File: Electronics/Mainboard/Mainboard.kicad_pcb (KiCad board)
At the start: 2 copper layers, 160 x 120 mm, 191 parts, among them J1 609-5192-ND, J2 DB25_Male_MountingHoles, J3 609-5192-ND, J4 609-5192-ND, U1 AD8676, U10 AD8675, U11 AD5781, U12 AD8676xR, U13 AD8675, U14 LM75C, U15 Beaglebone_Black, U16 AD5781, U17 AD8676xR, U18 AD8675, U19 ADP7142AUJZ-5.0, U2 AD8676, U20 ADR4550, U21 AD8676, U22 AD8675, U3 LT1469, U4 LTC2338-18, U5 AD5781, U6 AD8676xR, U7 AD8675, U8 AD5781, U9 AD8676xR

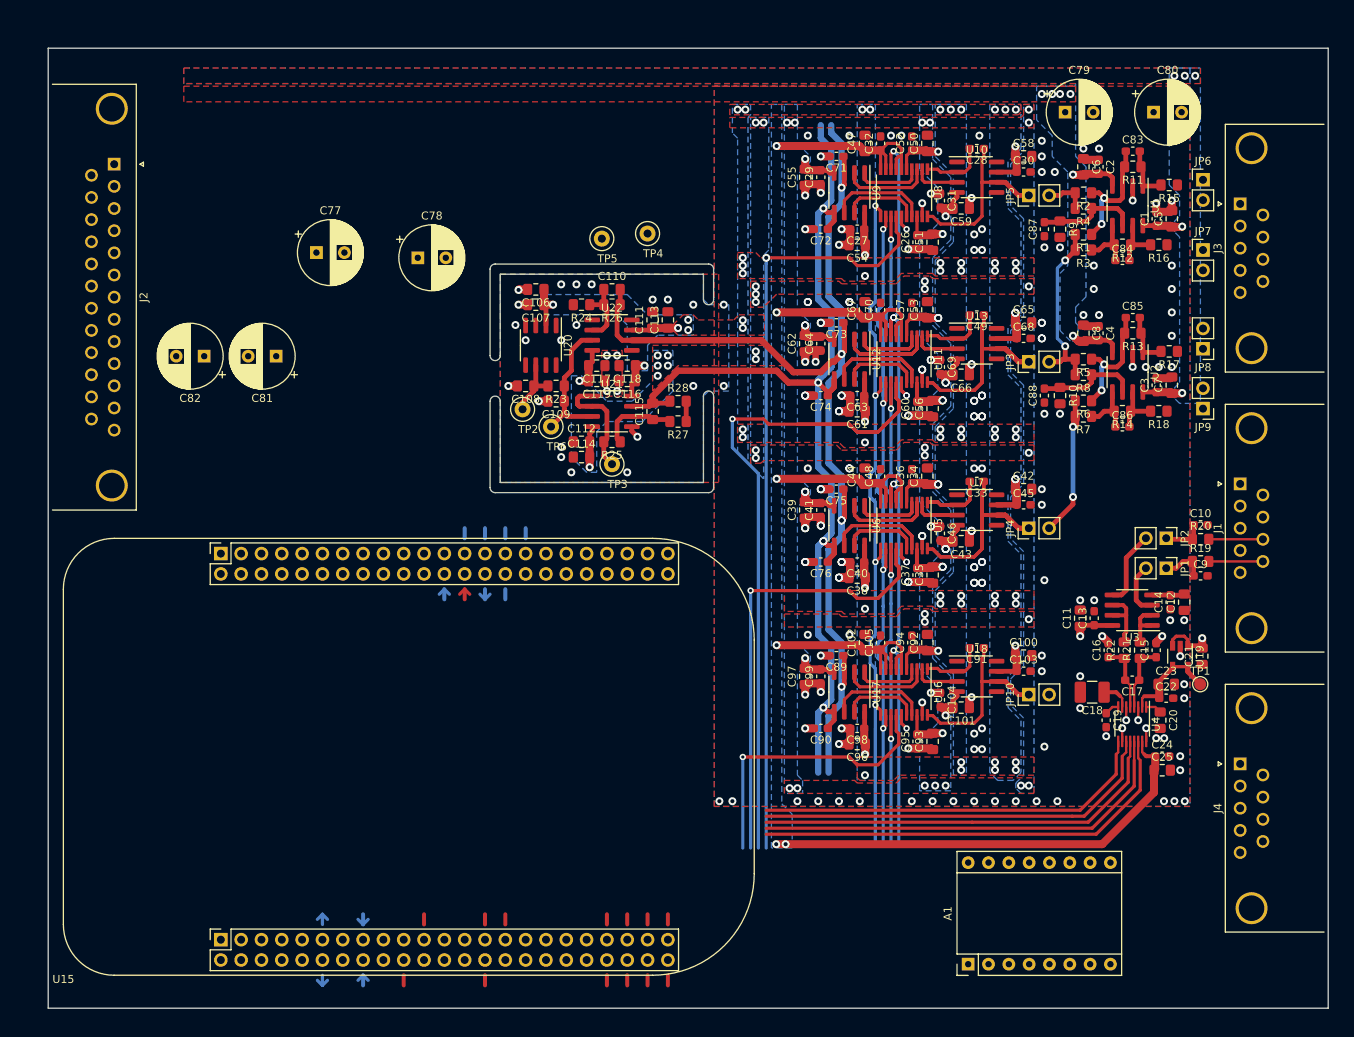
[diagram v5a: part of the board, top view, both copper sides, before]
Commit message: SPI Connections finished
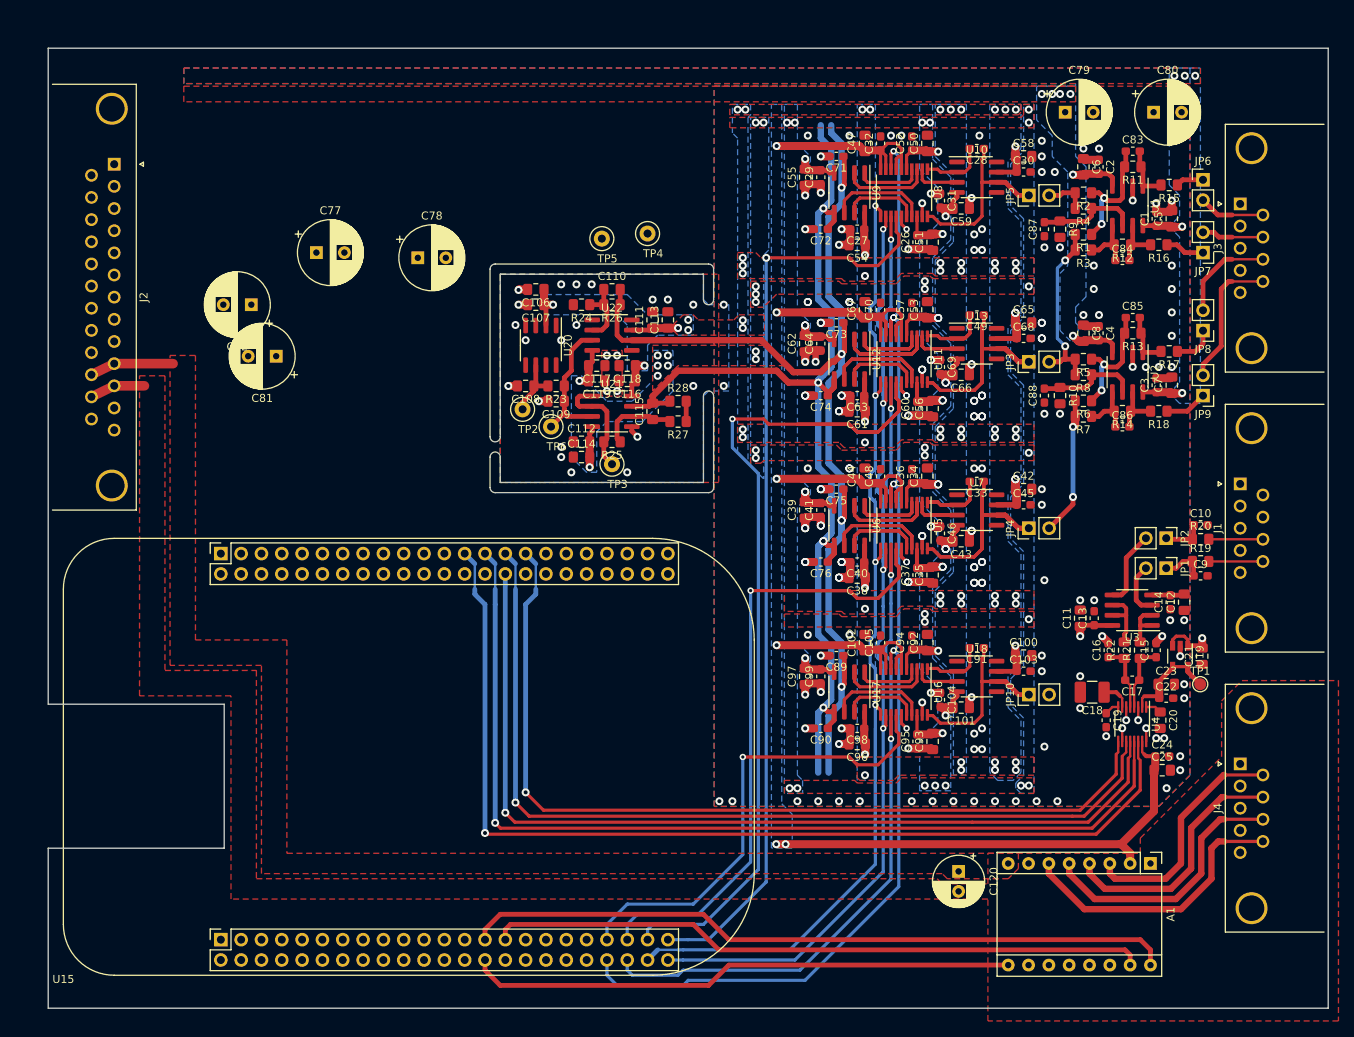
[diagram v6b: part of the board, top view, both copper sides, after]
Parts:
- added C120: 100u 35V, Capacitor_THT:CP_Radial_D6.3mm_P2.50mm, F.Cu at (183.8, 142.9)
- moved A1 26.0 mm to (207.8, 141.9), turned to 270 degrees
- moved C82 8.73 mm to (95.4, 72.1)
- moved JP8 2.28 mm to (214.3, 75.3)
- moved JP9 1.62 mm to (214.3, 83.4)
- moved JP7 0.33 mm to (214.3, 65.5), turned to 180 degrees
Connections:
- A1 pad 15: /Stepper-Driver/STEP -> /Beaglebone/Motor-Step
- J4 pad 6: /Stepper-Driver/B- -> /Stepper-Driver/A+
- J4 pad 7: /Stepper-Driver/B+ -> /Stepper-Driver/A-
- J4 pad 8: /Stepper-Driver/A- -> /Stepper-Driver/B+
- J4 pad 9: /Stepper-Driver/A+ -> /Stepper-Driver/B-
- U15 pad P8_27: Net-(U15-PadP8_27) -> /Stepper-Driver/DIR
- U15 pad P8_28: Net-(U15-PadP8_28) -> /Stepper-Driver/~ENABLE
- U15 pad P8_29: Net-(U15-PadP8_29) -> /Beaglebone/Motor-Step
- U15 pad P8_39: Net-(U15-PadP8_39) -> /~DAC_CS-Bias
- U15 pad P8_40: Net-(U15-PadP8_40) -> /~DAC_LDAC
- U15 pad P8_41: Net-(U15-PadP8_41) -> /~DAC_CS-Y
- U15 pad P8_42: Net-(U15-PadP8_42) -> /DAC_CLK
- U15 pad P8_43: Net-(U15-PadP8_43) -> /~DAC_CS-Z
- U15 pad P8_44: Net-(U15-PadP8_44) -> /DAC_MISO
- U15 pad P8_45: Net-(U15-PadP8_45) -> /~DAC_CS-X
- U15 pad P8_46: Net-(U15-PadP8_46) -> /DAC_MOSI
- U15 pad P9_25: Net-(U15-PadP9_25) -> /ADC_MISO
- U15 pad P9_27: Net-(U15-PadP9_27) -> /ADC_CLK
- U15 pad P9_29: Net-(U15-PadP9_29) -> /ADC_BUSY
- U15 pad P9_30: Net-(U15-PadP9_30) -> /ADC_MOSI
- U15 pad P9_31: Net-(U15-PadP9_31) -> /ADC_CONV
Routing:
- net /Stepper-Driver/DIR: track 0.00 -> 89.0 mm
- net /Beaglebone/Motor-Step: track 0.00 -> 82.5 mm
- net /ADC_MISO: track 55.2 -> 126.4 mm, vias 0 -> 1
- net /Stepper-Driver/~ENABLE: track 0.00 -> 68.5 mm
- net /ADC_CLK: track 53.8 -> 122.1 mm, vias 0 -> 1
- net /ADC_BUSY: track 51.3 -> 115.0 mm, vias 0 -> 1
- net /ADC_MOSI: track 52.5 -> 115.5 mm, vias 0 -> 1
- net /ADC_CONV: track 49.8 -> 111.7 mm, vias 0 -> 1
- net /~DAC_LDAC: track 106.3 -> 155.8 mm
- net (no net): track 44.3 -> 0.00 mm
- net /DAC_CLK: track 115.0 -> 159.1 mm
- net /DAC_MISO: track 132.8 -> 168.9 mm
- net /Stepper-Driver/B-: track 0.00 -> 35.6 mm
- net /DAC_MOSI: track 111.0 -> 146.1 mm
- net /Stepper-Driver/B+: track 0.00 -> 33.5 mm
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- added copper zone on F.Cu, net /9V
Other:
- outline, holes or cut-outs redrawn

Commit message: Further layout stuff
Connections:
- J1 pad 1: /+15V -> /-15V
- J1 pad 6: /-15V -> /+15V
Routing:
- net /Bias: track 0.00 -> 43.1 mm
- net /GND: track 156.9 -> 161.0 mm, vias 199 -> 205
- net /-15V: track 107.3 -> 109.5 mm, vias 56 -> 59
- net /+15V: vias 74 -> 80

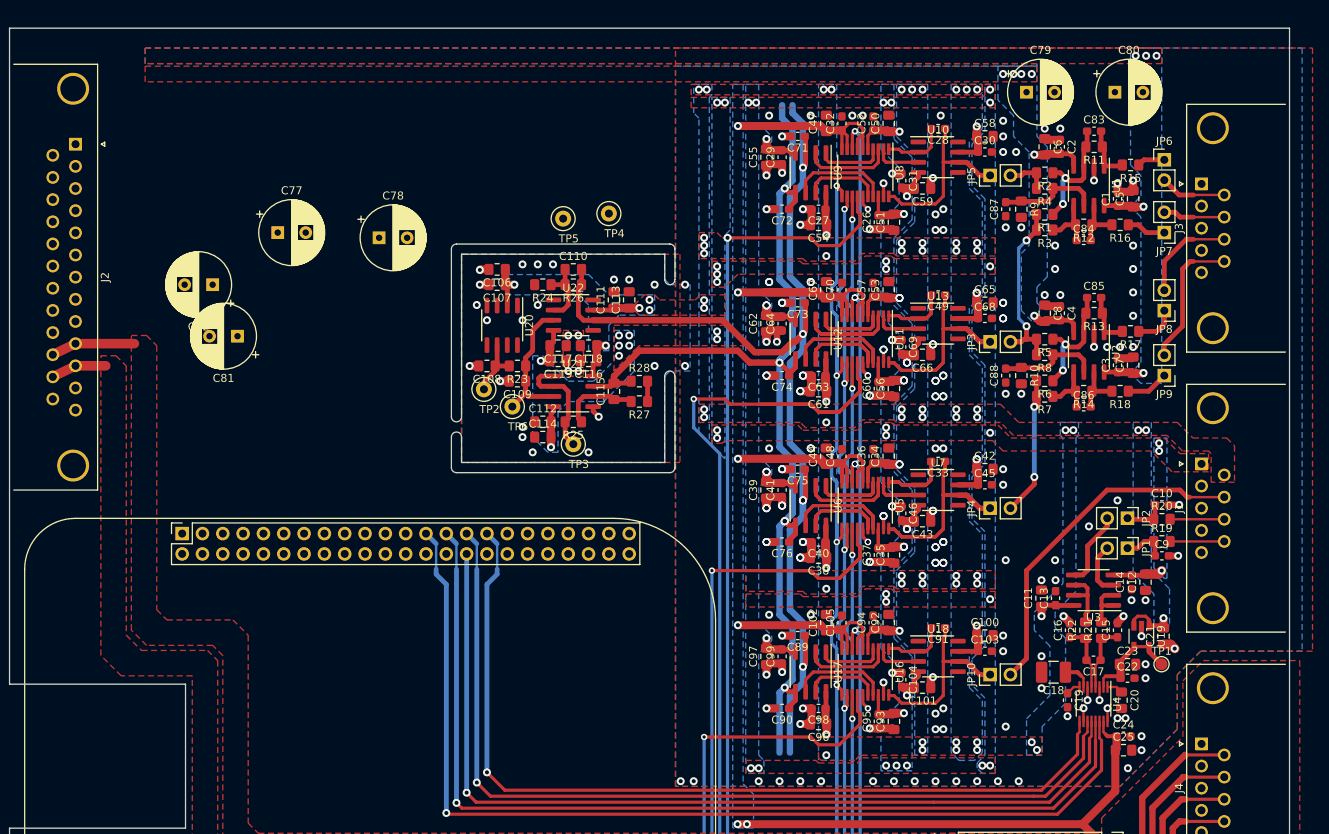
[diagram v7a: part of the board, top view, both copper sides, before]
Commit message: Power supply routing progress
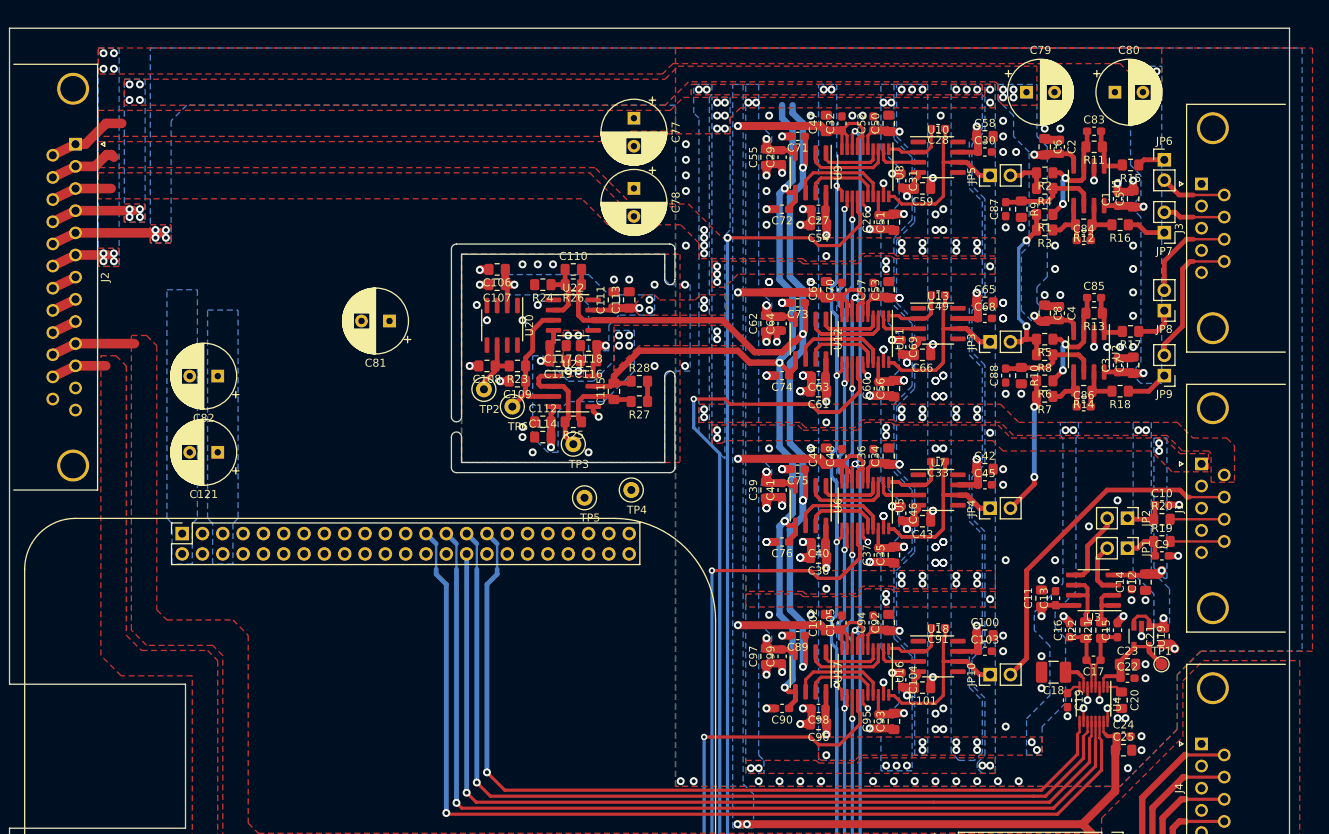
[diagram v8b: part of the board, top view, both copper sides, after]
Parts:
- added C121: 330u 16V, Capacitor_THT:CP_Radial_D8.0mm_P3.50mm, F.Cu at (96.0, 93.0)
- moved C77 46.8 mm to (148.1, 51.2), turned to 270 degrees
- moved TP5 35.0 mm to (141.9, 98.7)
- moved TP4 34.7 mm to (147.7, 97.7)
- moved C78 32.4 mm to (148.1, 60.0), turned to 270 degrees
- moved C81 19.1 mm to (117.5, 76.6)
- moved C82 11.4 mm to (96.0, 83.5)
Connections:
- C82 pad 1: /GND -> /5V
- C82 pad 2: /Beaglebone/5V -> /GND
- J2 pad 22: /Beaglebone/5V -> /5V
- J2 pad 9: /Beaglebone/5V -> /5V
- U15 pad P9_5: /Beaglebone/5V -> /5V
- U15 pad P9_6: /Beaglebone/5V -> /5V
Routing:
- net /GND: track 161.0 -> 186.6 mm, vias 205 -> 216
- net /REF_P: track 166.7 -> 155.3 mm
- net /-20V: track 12.8 -> 23.1 mm, vias 6 -> 14
- net /-15V: track 109.5 -> 119.9 mm, vias 59 -> 62
- net /REF_N: track 155.1 -> 146.7 mm
- net /+15V: track 129.4 -> 137.0 mm, vias 80 -> 81
- net /+20V: track 10.0 -> 17.2 mm, vias 5 -> 13
- net /3V3: track 212.6 -> 215.7 mm
- net /5V: track 0.00 -> 3.16 mm
- added copper zone on B.Cu, net /5V
